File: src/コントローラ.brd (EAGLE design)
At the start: 40 parts

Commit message: [add]コントローラ　Aoi
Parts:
- removed JP8: (no value), con-jst-xh (1):B3B-XH
- KAHEN: device pinhead:1X03 -> con-jst-xh (1):B3B-XH
- PIN, PINSOCKET: device pinhead:1X15 -> pinhead:1X07
- moved U$2 75.5 mm to (0.00, 146.1), turned to 270 degrees
- moved PINSOCKET 73.5 mm to (25.4, 143.5)
- moved R10 60.2 mm to (7.62, 121.9), turned to 270 degrees
- moved LED6 51.1 mm to (12.7, 127.0)
- moved R6 38.1 mm to (5.08, 104.1), turned to 270 degrees
- moved R8 34.9 mm to (2.54, 116.8), turned to 270 degrees
- moved R7 33.6 mm to (7.62, 106.7), turned to 270 degrees
- moved R9 32.4 mm to (5.08, 119.4), turned to 270 degrees
- moved LED4 28.4 mm to (27.9, 127.0)
- moved LED3 28.1 mm to (12.7, 111.8)
- moved LED1 25.2 mm to (14.0, 7.62), turned to 0 degrees
- moved LED2 22.7 mm to (20.3, 111.8)
- moved R5 19.4 mm to (14.0, 12.7), turned to 180 degrees
- moved LED5 18.5 mm to (20.3, 127.0)
- moved KAHEN 16.3 mm to (73.7, 68.6), turned to 0 degrees
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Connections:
- removed net AIN5: F303K8_R.6, JP8.2, KAHEN.2, LED6.2, PIN.14, PINSOCKET.14, R10.1
- removed net D1: F303K8_L.14, LED1.2, R5.1, TWE_R.14
- removed net N$1: PIN.3
- removed net N$8: PINSOCKET.3
- removed net SEL1: F303K8_L.5
- removed net SEL2: F303K8_L.6
- new net KN: F303K8_L.11, KAHEN.2, LED6.2, PIN.1, PINSOCKET.1
- new net N$10: LED5.1, R9.1
- new net N$11: LED4.1, R8.1
- new net N$4: LED1.1, R5.1
- new net N$5: LED2.1, R6.1
- new net N$7: LED3.1, R7.1
- new net N$9: LED6.1, R10.1
- new net TW: F303K8_L.13, LED1.2
- net 3V3: now also KAHEN.3, PIN.7, PINSOCKET.7; no longer JP8.3, KAHEN.1, PIN.15, PINSOCKET.15
- net BT_IN1: now also F303K8_L.5, PIN.5, PINSOCKET.5; no longer F303K8_L.9, PIN.7, PINSOCKET.7, R6.1
- net BT_IN2: now also F303K8_L.6, PIN.4, PINSOCKET.4; no longer F303K8_L.10, PIN.6, PINSOCKET.6, R7.1
- net GND: now also KAHEN.1, PIN.6, PINSOCKET.6; no longer JP8.1, KAHEN.3, LED1.1, LED2.1, LED3.1, LED4.1, LED5.1, LED6.1, PIN.13, PINSOCKET.13
- net SW_DOWN: now also F303K8_L.10, PIN.2, PINSOCKET.2; no longer F303K8_L.12, PIN.4, PINSOCKET.4, R9.1
- net SW_UP: now also F303K8_L.9, PIN.3, PINSOCKET.3; no longer F303K8_L.11, PIN.5, PINSOCKET.5, R8.1
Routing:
- net KN: track 0.00 -> 154.9 mm, vias 0 -> 4
- net AIN5: track 84.9 -> 0.00 mm, vias 2 -> 0
- net D1: track 63.5 -> 0.00 mm, vias 2 -> 0
- net TW: track 0.00 -> 53.3 mm
- net L/R1: track 113.9 -> 147.3 mm
- net BT_IN1: track 73.7 -> 106.7 mm
- net N$11: track 0.00 -> 30.5 mm
- net GND: track 498.0 -> 469.6 mm, vias 6 -> 4
- net SW_UP: track 114.3 -> 86.4 mm
- net SW_DOWN: track 116.8 -> 91.4 mm, vias 0 -> 2
- net 3V3: track 353.9 -> 331.5 mm, vias 4 -> 8
- net N$10: track 0.00 -> 17.8 mm
- net N$5: track 0.00 -> 17.8 mm
- net BT_IN2: track 86.4 -> 99.1 mm, vias 2 -> 0
- net U/D1: track 128.1 -> 136.7 mm
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
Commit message: [add]コントローラ　Aoi
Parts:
- moved U$1 117.9 mm to (94.0, 73.7), turned to 180 degrees
- moved C2 2.54 mm to (88.9, 52.1)
- moved TWE_L 2.54 mm to (47.0, 20.3)
- moved TWE_R 2.54 mm to (47.0, 5.08)
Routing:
- net 3V3: track 331.5 -> 340.5 mm
- net L/R1: track 147.3 -> 152.4 mm
- net TX: track 45.7 -> 48.3 mm
- net RX: track 40.6 -> 38.1 mm
- net GND: track 469.6 -> 472.2 mm
- net U/D1: vias 6 -> 4

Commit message: [add]コントローラ
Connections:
- removed net KN: F303K8_L.11, KAHEN.2, LED6.2, PIN.1, PINSOCKET.1
- new net KN1: F303K8_L.11, LED6.2, PIN.1, PINSOCKET.1
- new net KN2: F303K8_R.11, KAHEN.2
- new net N$1: JP2.1
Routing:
- net KN: track 154.9 -> 0.00 mm, vias 4 -> 0
- net KN1: track 0.00 -> 86.4 mm
- net KN2: track 0.00 -> 58.4 mm, vias 0 -> 2
- net 3V3: track 340.5 -> 377.5 mm, vias 8 -> 12
- net N$1: track 0.00 -> 5.08 mm, vias 0 -> 1
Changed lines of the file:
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@@
 </element>
 <element name="BUTTON" library="con-jst-xh" package="B2B-XH" value="02-JST" x="36.83" y="113.03" smashed="yes">
-<attribute name="NAME" x="35.56" y="116.84" size="1.27" layer="25"/>
+<attribute name="NAME" x="34.29" y="114.3" size="1.27" layer="25"/>
 <attribute name="VALUE" x="35.56" y="109.22" size="1.27" layer="27"/>
 </element>
@@
 <element name="U$1" library="prototyping-board" package="TYPE.B" value="" x="93.98" y="73.66" smashed="yes" rot="R180"/>
 <element name="BUTTON2" library="con-jst-xh" package="B2B-XH" value="02-JST" x="29.21" y="113.03" smashed="yes">
-<attribute name="NAME" x="27.94" y="116.84" size="1.27" layer="25"/>
+<attribute name="NAME" x="25.4" y="114.3" size="1.27" layer="25"/>
 <attribute name="VALUE" x="27.94" y="109.22" size="1.27" layer="27"/>
 </element>
@@
 </element>
 <element name="LED1" library="con-jst-xh (1)" package="B2B-XH" value="02-JST" x="13.97" y="7.62" smashed="yes">
-<attribute name="NAME" x="12.7" y="11.43" size="1.27" layer="26" rot="MR180"/>
+<attribute name="NAME" x="17.78" y="3.81" size="1.27" layer="25" rot="R180"/>
 <attribute name="VALUE" x="12.7" y="3.81" size="1.27" layer="27"/>
 </element>
 <element name="R5" library="rcl" library_urn="urn:adsk.eagle:library:334" package="0204/7" package3d_urn="urn:adsk.eagle:package:23498/2" value="100" x="13.97" y="12.7" smashed="yes" rot="R180">
-<attribute name="NAME" x="16.51" y="11.4046" size="0.9906" layer="25" ratio="10" rot="R180"/>
+<attribute name="NAME" x="15.24" y="13.9446" size="0.9906" layer="25" ratio="10" rot="R180"/>
 <attribute name="POPULARITY" value="79" x="13.97" y="12.7" size="1.778" layer="27" rot="R180" display="off"/>
 <attribute name="SPICEPREFIX" value="R" x="13.97" y="12.7" size="1.778" layer="27" rot="R180" display="off"/>
@@
 </element>
 <element name="LED2" library="con-jst-xh (1)" package="B2B-XH" value="02-JST" x="20.32" y="111.76" smashed="yes" rot="R270">
-<attribute name="NAME" x="24.13" y="113.03" size="1.27" layer="25" rot="R270"/>
+<attribute name="NAME" x="21.59" y="114.3" size="1.27" layer="25" rot="R270"/>
 <attribute name="VALUE" x="16.51" y="113.03" size="1.27" layer="27" rot="R270"/>
 </element>
@@
 </element>
 <element name="LED3" library="con-jst-xh (1)" package="B2B-XH" value="02-JST" x="12.7" y="111.76" smashed="yes" rot="R270">
-<attribute name="NAME" x="16.51" y="113.03" size="1.27" layer="25" rot="R270"/>
+<attribute name="NAME" x="13.97" y="114.3" size="1.27" layer="25" rot="R270"/>
 <attribute name="VALUE" x="8.89" y="113.03" size="1.27" layer="27" rot="R270"/>
 </element>
@@
 </element>
 <element name="LED4" library="con-jst-xh (1)" package="B2B-XH" value="02-JST" x="27.94" y="127" smashed="yes" rot="R270">
-<attribute name="NAME" x="31.75" y="128.27" size="1.27" layer="25" rot="R270"/>
+<attribute name="NAME" x="29.21" y="129.54" size="1.27" layer="25" rot="R270"/>
 <attribute name="VALUE" x="24.13" y="128.27" size="1.27" layer="27" rot="R270"/>
 </element>
@@
 </element>
 <element name="LED5" library="con-jst-xh (1)" package="B2B-XH" value="02-JST" x="20.32" y="127" smashed="yes" rot="R270">
-<attribute name="NAME" x="24.13" y="128.27" size="1.27" layer="25" rot="R270"/>
+<attribute name="NAME" x="21.59" y="129.54" size="1.27" layer="25" rot="R270"/>
 <attribute name="VALUE" x="16.51" y="128.27" size="1.27" layer="27" rot="R270"/>
 </element>
@@
 </element>
 <element name="LED6" library="con-jst-xh (1)" package="B2B-XH" value="02-JST" x="12.7" y="127" smashed="yes" rot="R270">
-<attribute name="NAME" x="16.51" y="128.27" size="1.27" layer="25" rot="R270"/>
+<attribute name="NAME" x="13.97" y="129.54" size="1.27" layer="25" rot="R270"/>
 <attribute name="VALUE" x="10.16" y="129.54" size="1.27" layer="27" rot="R270"/>
 </element>
@@
 <via x="83.82" y="53.34" extent="1-16" drill="0.35"/>
 <wire x1="66.04" y1="33.02" x2="76.2" y2="33.02" width="0.1524" layer="16"/>
+<via x="76.2" y="33.02" extent="1-16" drill="0.35"/>
+<via x="76.2" y="12.7" extent="1-16" drill="0.35"/>
+<wire x1="76.2" y1="33.02" x2="76.2" y2="12.7" width="0.1524" layer="1"/>
+<via x="76.2" y="33.02" extent="1-16" drill="0.35"/>
+<via x="15.24" y="45.72" extent="1-16" drill="0.35"/>
+<wire x1="24.227675" y1="46.7106" x2="26.572325" y2="46.7106" width="0.1524" layer="1"/>
+<wire x1="15.24" y1="45.72" x2="23.237075" y2="45.72" width="0.1524" layer="1"/>
+<wire x1="23.237075" y1="45.72" x2="24.227675" y2="46.7106" width="0.1524" layer="1"/>
+<wire x1="29.8732" y1="43.409725" x2="29.8732" y2="43.18" width="0.1524" layer="1"/>
+<wire x1="26.572325" y1="46.7106" x2="29.8732" y2="43.409725" width="0.1524" layer="1"/>
 <wire x1="33.02" y1="71.12" x2="35.56" y2="107.95" width="0" layer="19" extent="1-1"/>
-<wire x1="76.2" y1="12.7" x2="76.2" y2="33.02" width="0" layer="19" extent="16-16"/>
 </signal>
 <signal name="TX">
@@
 <wire x1="27.94" y1="120.65" x2="2.54" y2="120.65" width="0.1524" layer="16"/>
 </signal>
-<signal name="KN">
-<contactref element="KAHEN" pad="2"/>
-<contactref element="LED6" pad="2"/>
-<contactref element="F303K8_L" pad="11"/>
-<contactref element="PIN" pad="1"/>
-<wire x1="17.78" y1="71.12" x2="12.7" y2="71.12" width="0.1524" layer="16"/>
-<wire x1="12.7" y1="71.12" x2="12.7" y2="55.88" width="0.1524" layer="16"/>
-<wire x1="12.7" y1="55.88" x2="25.4" y2="55.88" width="0.1524" layer="16"/>
-<wire x1="73.66" y1="66.04" x2="68.58" y2="66.04" width="0.1524" layer="16"/>
-<wire x1="73.66" y1="68.58" x2="73.66" y2="66.04" width="0.1524" layer="16"/>
-<wire x1="68.58" y1="68.58" x2="50.8" y2="68.58" width="0.1524" layer="16"/>
-<wire x1="45.72" y1="40.64" x2="38.1" y2="40.64" width="0.1524" layer="16"/>
-<via x="45.72" y="40.64" extent="1-16" drill="0.35"/>
-<via x="50.8" y="68.58" extent="1-16" drill="0.35"/>
-<wire x1="68.58" y1="68.58" x2="68.58" y2="66.04" width="0.1524" layer="16"/>
-<contactref element="PINSOCKET" pad="1"/>
-<wire x1="17.78" y1="143.51" x2="12.7" y2="143.51" width="0.1524" layer="16"/>
-<wire x1="12.7" y1="143.51" x2="12.7" y2="128.27" width="0.1524" layer="16"/>
-<wire x1="50.8" y1="60.96" x2="50.8" y2="40.64" width="0.1524" layer="16"/>
-<via x="50.8" y="40.64" extent="1-16" drill="0.35"/>
-<via x="50.8" y="60.96" extent="1-16" drill="0.35"/>
-<wire x1="50.8" y1="68.58" x2="50.8" y2="60.96" width="0.1524" layer="1"/>
-<wire x1="50.8" y1="40.64" x2="45.72" y2="40.64" width="0.1524" layer="1"/>
-<wire x1="38.1" y1="40.64" x2="22.86" y2="40.64" width="0.1524" layer="16"/>
-<wire x1="22.86" y1="40.64" x2="22.86" y2="48.26" width="0.1524" layer="16"/>
-<wire x1="22.86" y1="48.26" x2="25.4" y2="48.26" width="0.1524" layer="16"/>
-<wire x1="25.4" y1="48.26" x2="25.4" y2="55.88" width="0.1524" layer="16"/>
-<wire x1="17.78" y1="71.12" x2="12.7" y2="128.27" width="0" layer="19" extent="1-1"/>
-</signal>
 <signal name="TW">
 <contactref element="LED1" pad="2"/>
@@
 <wire x1="12.7" y1="15.24" x2="20.32" y2="15.24" width="0.1524" layer="16"/>
 </signal>
+<signal name="KN1">
+<contactref element="F303K8_L" pad="11"/>
+<contactref element="LED6" pad="2"/>
+<contactref element="PINSOCKET" pad="1"/>
+<wire x1="12.7" y1="143.51" x2="17.78" y2="143.51" width="0.1524" layer="16"/>
+<contactref element="PIN" pad="1"/>
+<wire x1="17.78" y1="71.12" x2="12.7" y2="71.12" width="0.1524" layer="16"/>
+<wire x1="12.7" y1="71.12" x2="12.7" y2="55.88" width="0.1524" layer="16"/>
+<wire x1="12.7" y1="55.88" x2="25.4" y2="55.88" width="0.1524" layer="16"/>
+<wire x1="22.86" y1="48.26" x2="22.86" y2="40.64" width="0.1524" layer="16"/>
+<wire x1="22.86" y1="48.26" x2="25.4" y2="48.26" width="0.1524" layer="16"/>
+<wire x1="25.4" y1="48.26" x2="25.4" y2="55.88" width="0.1524" layer="16"/>
+<wire x1="22.86" y1="40.64" x2="38.1" y2="40.64" width="0.1524" layer="16"/>
+<wire x1="12.7" y1="128.27" x2="12.7" y2="143.51" width="0.1524" layer="16"/>
+<wire x1="17.78" y1="71.12" x2="12.7" y2="128.27" width="0" layer="19" extent="1-1"/>
+</signal>
+<signal name="KN2">
+<contactref element="F303K8_R" pad="11"/>
+<contactref element="KAHEN" pad="2"/>
+<wire x1="73.66" y1="66.04" x2="68.58" y2="66.04" width="0.1524" layer="16"/>
+<wire x1="73.66" y1="68.58" x2="73.66" y2="66.04" width="0.1524" layer="16"/>
+<wire x1="68.58" y1="68.58" x2="50.8" y2="68.58" width="0.1524" layer="16"/>
+<via x="50.8" y="68.58" extent="1-16" drill="0.35"/>
+<wire x1="68.58" y1="68.58" x2="68.58" y2="66.04" width="0.1524" layer="16"/>
+<wire x1="50.8" y1="40.64" x2="50.8" y2="60.96" width="0.1524" layer="16"/>
+<via x="50.8" y="60.96" extent="1-16" drill="0.35"/>
+<wire x1="50.8" y1="68.58" x2="50.8" y2="60.96" width="0.1524" layer="1"/>
+<wire x1="53.34" y1="40.64" x2="50.8" y2="40.64" width="0.1524" layer="16"/>
+</signal>
+<signal name="N$1">
+<contactref element="JP2" pad="1"/>
+<wire x1="25.4" y1="43.18" x2="30.48" y2="43.18" width="0.1524" layer="16"/>
+<via x="30.48" y="43.18" extent="1-16" drill="0.35"/>
+</signal>
 </signals>

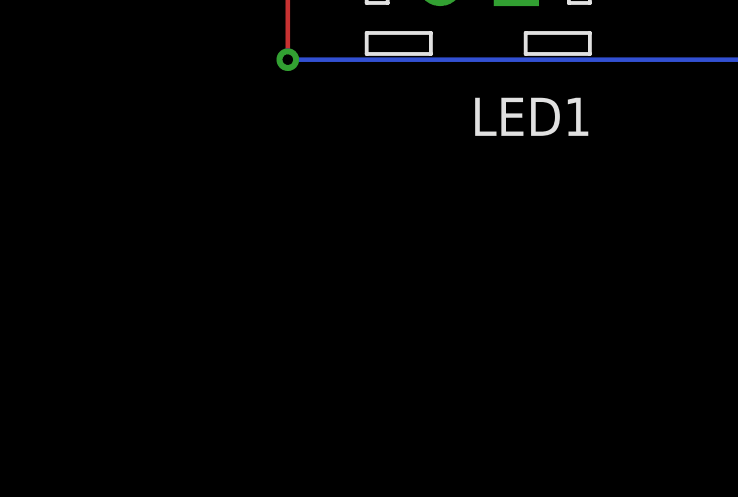
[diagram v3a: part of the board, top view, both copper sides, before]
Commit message: 国技館コントローラの追加
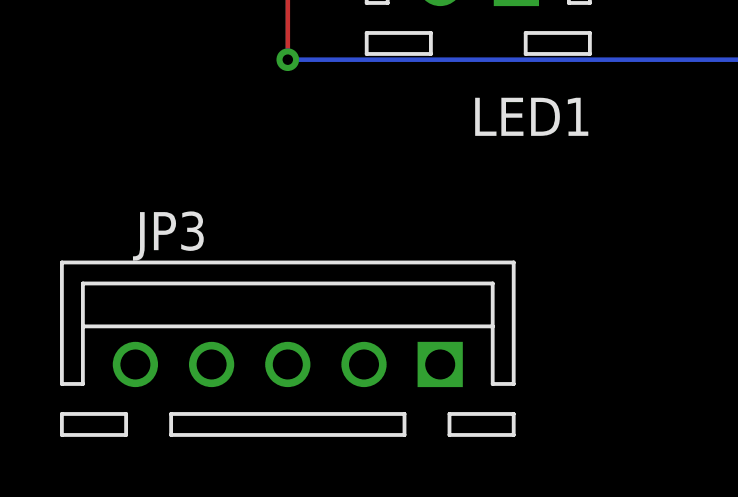
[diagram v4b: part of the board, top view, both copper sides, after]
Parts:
- added JP3: (no value), con-jst-xh:B5B-XH
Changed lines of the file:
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@@
 <attribute name="VALUE" x="16.51" y="140.335" size="1.27" layer="27"/>
+</element>
+<element name="JP3" library="con-jst-xh" package="B5B-XH" value="" x="7.62" y="-5.08" smashed="yes">
+<attribute name="NAME" x="2.54" y="-1.27" size="1.27" layer="25"/>
+<attribute name="VALUE" x="2.54" y="-8.89" size="1.27" layer="27"/>
 </element>
 </elements>
